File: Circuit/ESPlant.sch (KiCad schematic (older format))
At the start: 48 parts, among them P1 SOIL, P101 CONN_DIGITAL, P102 CONN_ANALOG, P103 CONN_SERIAL, P104 CONN_I2C, P105 SOLAR, P106 USB_5PIN_SHELL, P109 CONN_PWR, P110 CONN_01X05, P111 UV, P112 TEMP, P113 NEOPIXEL, P114 PIR, Q101 FDN340P, SW101 RESET, SW102 PRGM, SW103 RESET, U101 STM32F042F, U103 ESP-12E

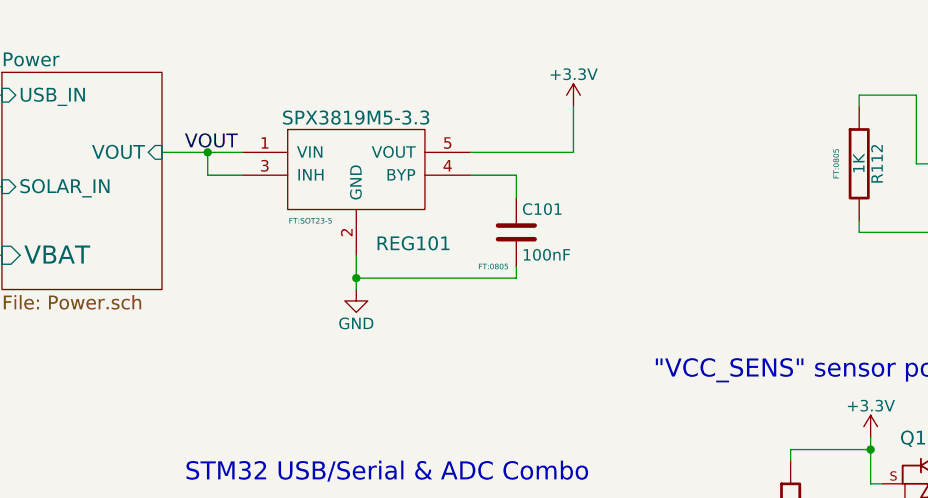
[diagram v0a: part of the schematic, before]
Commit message: Add power switch to schematic, SS12D00 switch footprint
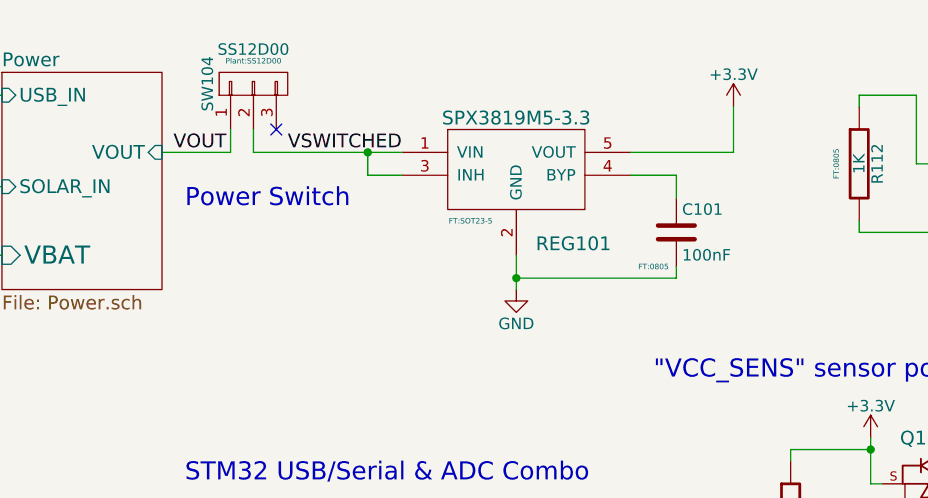
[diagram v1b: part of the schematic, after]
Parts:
- added SW104: SS12D00, Plant:SS12D00, symbol CONN_01X03
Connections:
- net labels added: VSWITCHED
- wire segments 165 -> 168
- no-connect marks 12 -> 13
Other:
- note added: "Power Switch"
- moved on the sheet: C101, REG101
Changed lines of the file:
@@
 L LD3985M-RESCUE-ESPlant REG101
 U 1 1 564B2BD1
-P 4300 1150
-F 0 "REG101" H 4550 800 60  0000 C CNN
-F 1 "SPX3819M5-3.3" H 4300 1350 60  0000 C CNN
-F 2 "FT:SOT23-5" H 4100 900 24  0000 C CNN
-F 3 "" H 4300 1150 60  0000 C CNN
-	1    4300 1150
+P 5000 1150
+F 0 "REG101" H 5250 800 60  0000 C CNN
+F 1 "SPX3819M5-3.3" H 5000 1350 60  0000 C CNN
+F 2 "FT:SOT23-5" H 4800 900 24  0000 C CNN
+F 3 "" H 5000 1150 60  0000 C CNN
+	1    5000 1150
 	1    0    0    -1
 $EndComp
@@
 L +3.3V #PWR114
 U 1 1 564B2FF9
-P 5250 900
-F 0 "#PWR114" H 5250 750 50  0001 C CNN
-F 1 "+3.3V" H 5250 1040 50  0000 C CNN
-F 2 "" H 5250 900 60  0000 C CNN
-F 3 "" H 5250 900 60  0000 C CNN
-	1    5250 900
-	1    0    0    -1
-$EndComp
-$Comp
-L GND #PWR110
+P 5950 900
+F 0 "#PWR114" H 5950 750 50  0001 C CNN
+F 1 "+3.3V" H 5950 1040 50  0000 C CNN
+F 2 "" H 5950 900 60  0000 C CNN
+F 3 "" H 5950 900 60  0000 C CNN
+	1    5950 900
+	1    0    0    -1
+$EndComp
+$Comp
+L GND #PWR112
 U 1 1 564B3125
-P 4300 1700
-F 0 "#PWR110" H 4300 1450 50  0001 C CNN
-F 1 "GND" H 4300 1550 50  0000 C CNN
-F 2 "" H 4300 1700 60  0000 C CNN
-F 3 "" H 4300 1700 60  0000 C CNN
-	1    4300 1700
+P 5000 1700
+F 0 "#PWR112" H 5000 1450 50  0001 C CNN
+F 1 "GND" H 5000 1550 50  0000 C CNN
+F 2 "" H 5000 1700 60  0000 C CNN
+F 3 "" H 5000 1700 60  0000 C CNN
+	1    5000 1700
 	1    0    0    -1
 $EndComp
@@
 L C C101
 U 1 1 564BAF1F
-P 5000 1450
-F 0 "C101" H 5025 1550 50  0000 L CNN
-F 1 "100nF" H 5025 1350 50  0000 L CNN
-F 2 "FT:0805" H 4900 1300 24  0000 C CNN
-F 3 "" H 5000 1450 60  0000 C CNN
-	1    5000 1450
+P 5700 1450
+F 0 "C101" H 5725 1550 50  0000 L CNN
+F 1 "100nF" H 5725 1350 50  0000 L CNN
+F 2 "FT:0805" H 5600 1300 24  0000 C CNN
+F 3 "" H 5700 1450 60  0000 C CNN
+	1    5700 1450
 	1    0    0    -1
 $EndComp
@@
 	1    0    0    -1
 $EndComp
-Text Label 3550 1100 0    60   ~ 0
+Text Label 3500 1100 0    60   ~ 0
 VOUT
 Text Label 6700 4100 1    60   ~ 0
@@
 STM_SWCLK
 $Comp
-L GND #PWR112
+L GND #PWR111
 U 1 1 564EA3B7
 P 4550 5300
-F 0 "#PWR112" H 4550 5050 50  0001 C CNN
+F 0 "#PWR111" H 4550 5050 50  0001 C CNN
 F 1 "GND" H 4550 5150 50  0000 C CNN
 F 2 "" H 4550 5300 60  0000 C CNN
@@
 $EndComp
 $Comp
-L +3.3V #PWR111
+L +3.3V #PWR110
 U 1 1 564EA803
 P 4450 2800
-F 0 "#PWR111" H 4450 2650 50  0001 C CNN
+F 0 "#PWR110" H 4450 2650 50  0001 C CNN
 F 1 "+3.3V" H 4450 2940 50  0000 C CNN
 F 2 "" H 4450 2800 60  0000 C CNN
@@
 Wire Wire Line
 	10050 5050 10050 4900
-Connection ~ 4300 1650
-Wire Wire Line
-	5000 1650 4300 1650
-Wire Wire Line
-	5000 1600 5000 1650
-Wire Wire Line
-	5000 1200 4800 1200
-Wire Wire Line
-	5000 1300 5000 1200
+Connection ~ 5000 1650
+Wire Wire Line
+	5700 1650 5000 1650
+Wire Wire Line
+	5700 1600 5700 1650
+Wire Wire Line
+	5700 1200 5500 1200
+Wire Wire Line
+	5700 1300 5700 1200
 Wire Wire Line
 	1300 950  1650 950
@@
 	2450 1250 2750 1250
 Wire Wire Line
-	4300 1550 4300 1700
-Wire Wire Line
-	5250 1100 5250 900
-Wire Wire Line
-	4800 1100 5250 1100
-Connection ~ 3650 1100
-Wire Wire Line
-	3650 1200 3650 1100
-Wire Wire Line
-	3800 1200 3650 1200
-Wire Wire Line
-	3450 1100 3800 1100
+	5000 1550 5000 1700
+Wire Wire Line
+	5950 1100 5950 900
+Wire Wire Line
+	5500 1100 5950 1100
+Connection ~ 4350 1100
+Wire Wire Line
+	4350 1200 4350 1100
+Wire Wire Line
+	4500 1200 4350 1200
+Wire Wire Line
+	3850 1100 4500 1100
 Wire Wire Line
 	1450 2450 1450 2650
@@
 GPIO2
 Connection ~ 9600 5900
+$Comp
+L CONN_01X03 SW104
+U 1 1 566DF313
+P 3850 800
+F 0 "SW104" H 3850 1000 50  0000 C CNN
+F 1 "SS12D00" V 4000 800 50  0000 C CNN
+F 2 "Plant:SS12D00" V 3950 800 24  0000 C CNN
+F 3 "" H 3850 800 60  0000 C CNN
+	1    3850 800
+	0    -1   -1   0
+$EndComp
+Wire Wire Line
+	3450 1100 3750 1100
+Wire Wire Line
+	3750 1100 3750 1000
+Wire Wire Line
+	3850 1000 3850 1100
+NoConn ~ 3950 1000
+Text Notes 3550 1350 0    79   ~ 0
+Power Switch
+Text Label 4000 1100 0    60   ~ 0
+VSWITCHED
 $EndSCHEMATC

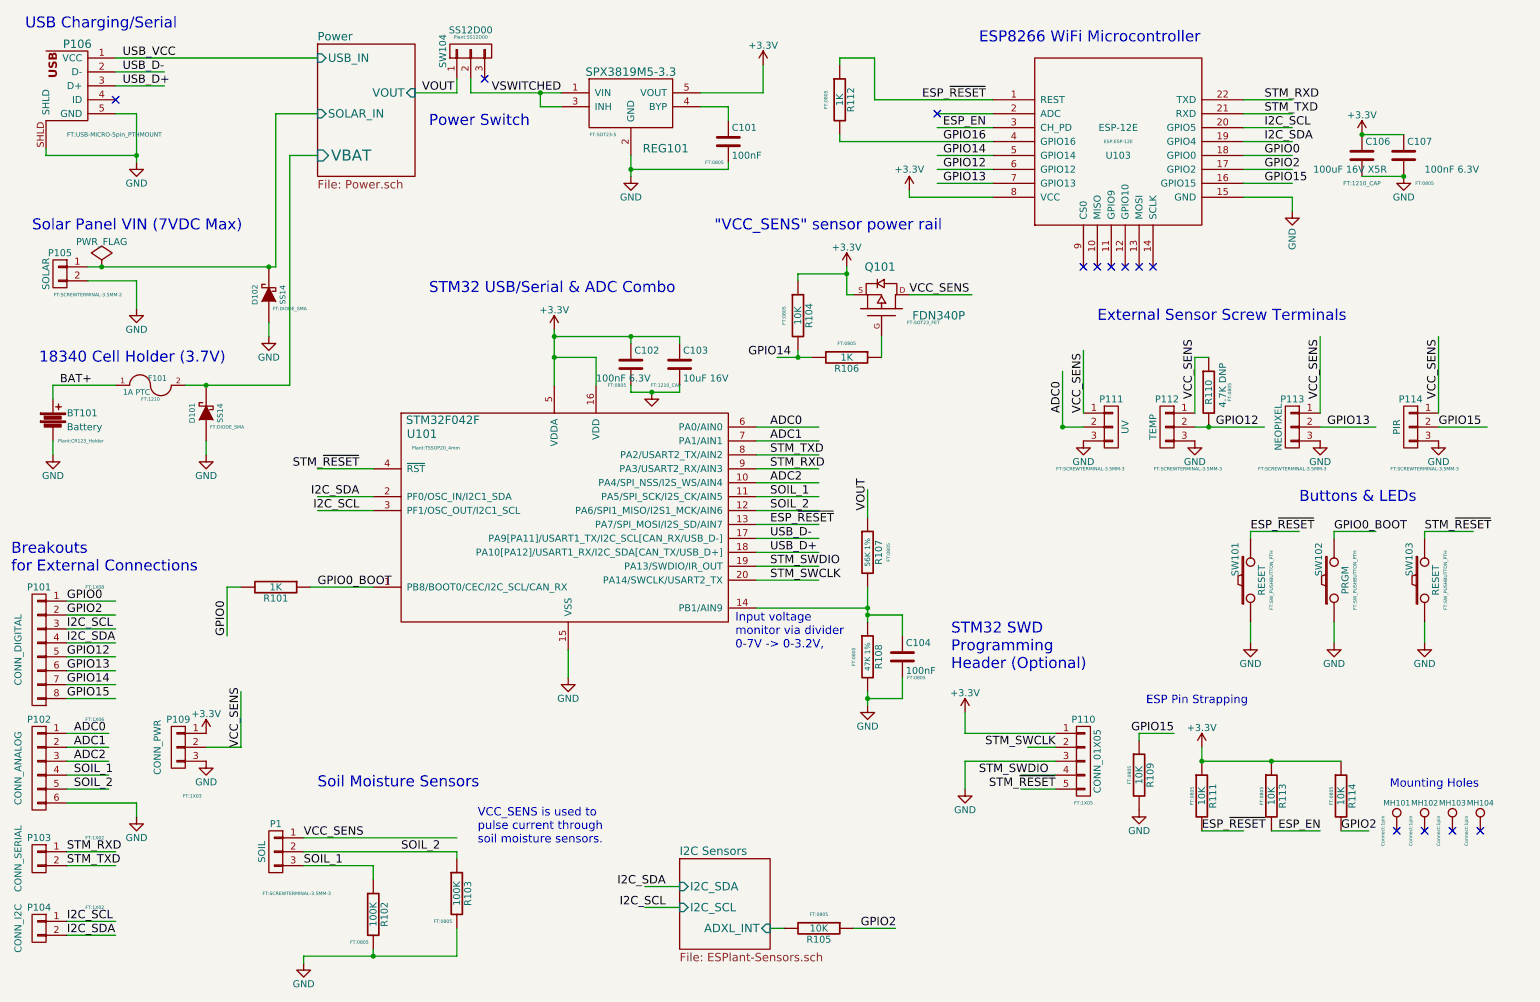
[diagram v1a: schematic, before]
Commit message: Downsize 0805s to 0603 for @jonoxer's pnp machine :)
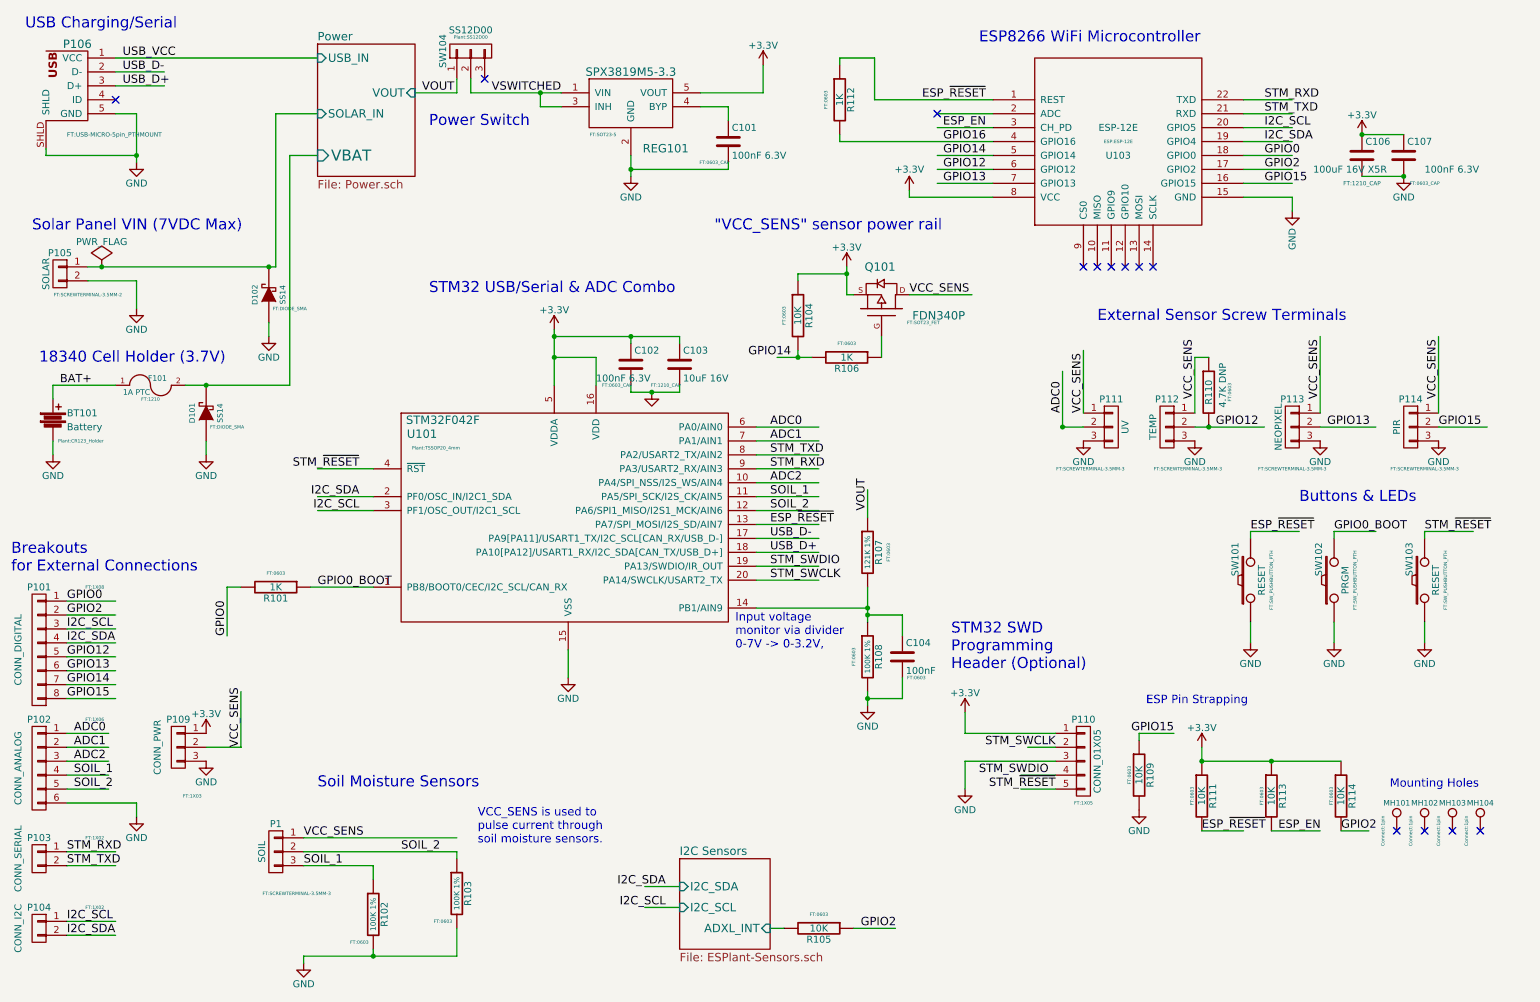
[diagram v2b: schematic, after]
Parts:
- C101: value 100nF -> 100nF 6.3V; footprint FT:0805 -> FT:0603_CAP
- C102, C107: footprint FT:0805 -> FT:0603_CAP
- C104, R104, R105, R106, R109, R110, R111, R112, R113, R114: footprint FT:0805 -> FT:0603
- R101: footprint (none) -> FT:0603
- R102, R103: value 100K -> 100K 1%; footprint FT:0805 -> FT:0603
- R107: value 56K 1% -> 121K 1%; footprint FT:0805 -> FT:0603
- R108: value 47K 1% -> 100K 1%; footprint FT:0805 -> FT:0603

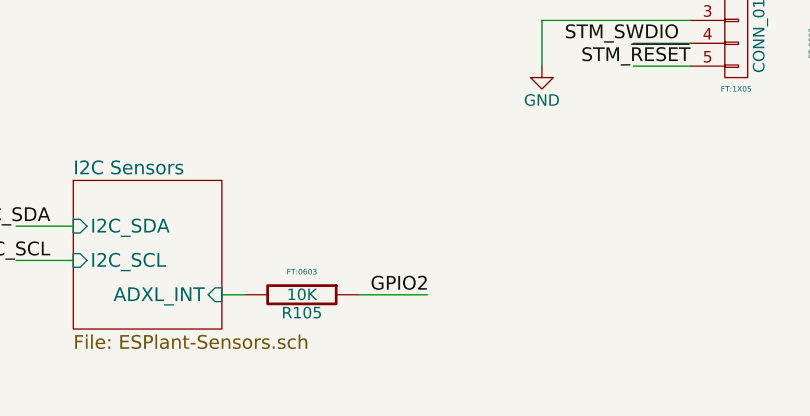
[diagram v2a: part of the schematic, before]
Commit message: V1.1 reroutes, excluding 0805->0603
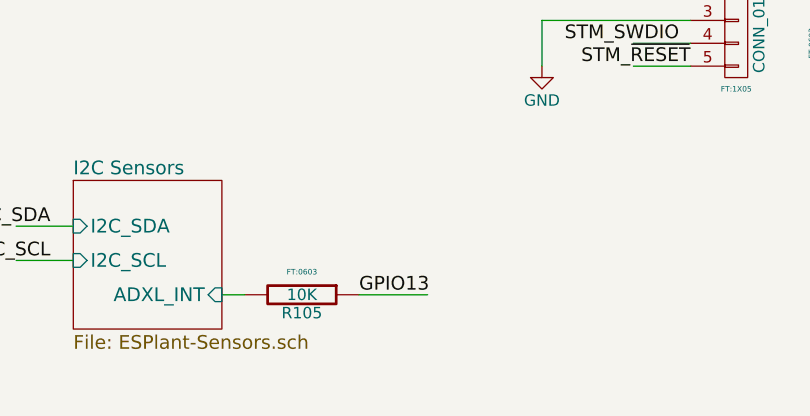
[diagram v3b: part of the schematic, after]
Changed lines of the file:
@@
 	0    1    1    0
 $EndComp
-Text Label 6650 7100 0    60   ~ 0
-GPIO2
+Text Label 6600 7100 0    60   ~ 0
+GPIO13
 $Comp
 L STM32F042F U101

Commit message: Shrink to 0603, some other cleanups
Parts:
- C104: footprint FT:0603 -> FT:0603_CAP
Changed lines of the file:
@@
 F 0 "C104" H 6975 5250 50  0000 L CNN
 F 1 "100nF" H 6975 5050 50  0000 L CNN
-F 2 "FT:0603" H 7050 5000 24  0000 C CNN
+F 2 "FT:0603_CAP" H 7050 5000 24  0000 C CNN
 F 3 "" H 6950 5150 60  0000 C CNN
 	1    6950 5150
@@
 Wire Wire Line
 	950  6650 1300 6650
+Text Label 950  4950 0    60   ~ 0
+I2C_SDA
 Text Label 950  5050 0    60   ~ 0
-I2C_SDA
-Text Label 950  4950 0    60   ~ 0
 I2C_SCL
 Text Label 950  4750 0    60   ~ 0

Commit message: Battery is a 16340 cell not an 18340 cell
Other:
- note added: "16340 Cell Holder (3.7V)\n"
- note removed: "18340 Cell Holder (3.7V)\n"
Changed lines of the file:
@@
 $EndComp
 Text Notes 750  3050 0    79   ~ 0
-18340 Cell Holder (3.7V)\n
+16340 Cell Holder (3.7V)\n
 $Comp
 L GND #PWR011

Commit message: Fix silkscreen & slot width issues noted by @hackvana, bump version V1.3
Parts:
- C101, C102, C107: value 100nF 6.3V -> 100nF
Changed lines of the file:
@@
 P 10550 1550
 F 0 "C107" H 10575 1650 50  0000 L CNN
-F 1 "100nF 6.3V" H 10700 1450 50  0000 L CNN
+F 1 "100nF" H 10700 1450 50  0000 L CNN
 F 2 "FT:0603_CAP" H 10700 1350 24  0000 C CNN
 F 3 "" H 10550 1550 60  0000 C CNN
@@
 P 5700 1450
 F 0 "C101" H 5725 1550 50  0000 L CNN
-F 1 "100nF 6.3V" H 5725 1350 50  0000 L CNN
+F 1 "100nF" H 5725 1350 50  0000 L CNN
 F 2 "FT:0603_CAP" H 5600 1300 24  0000 C CNN
 F 3 "" H 5700 1450 60  0000 C CNN
@@
 P 5000 3050
 F 0 "C102" H 5025 3150 50  0000 L CNN
-F 1 "100nF 6.3V" H 4750 2950 50  0000 L CNN
+F 1 "100nF" H 4750 2950 50  0000 L CNN
 F 2 "FT:0603_CAP" H 4900 2900 24  0000 C CNN
 F 3 "" H 5000 3050 60  0000 C CNN
